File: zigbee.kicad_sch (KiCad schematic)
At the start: 49 parts, among them J201 Conn_Coaxial, J202 Conn_Coaxial, U201 0900PC15A0036E, U202 CC2652P1FRGZR, U203 CC2652P1FRGZR, X201 Crystal, X202 Crystal_GND24

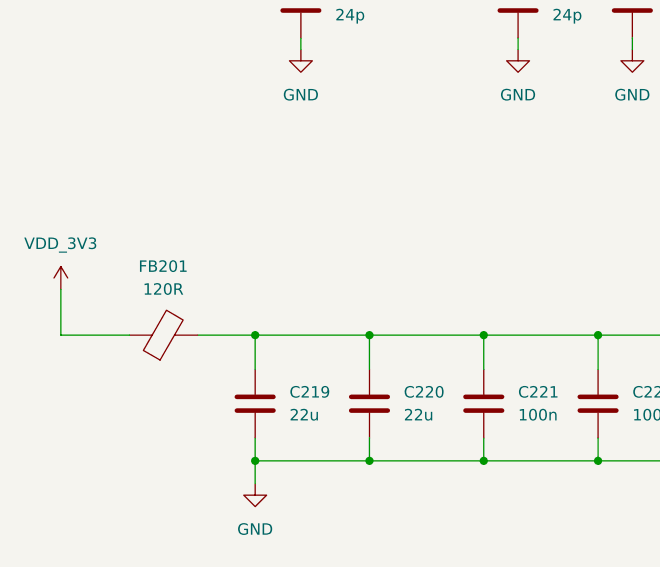
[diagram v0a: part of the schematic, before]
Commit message: Added more thread circuitry
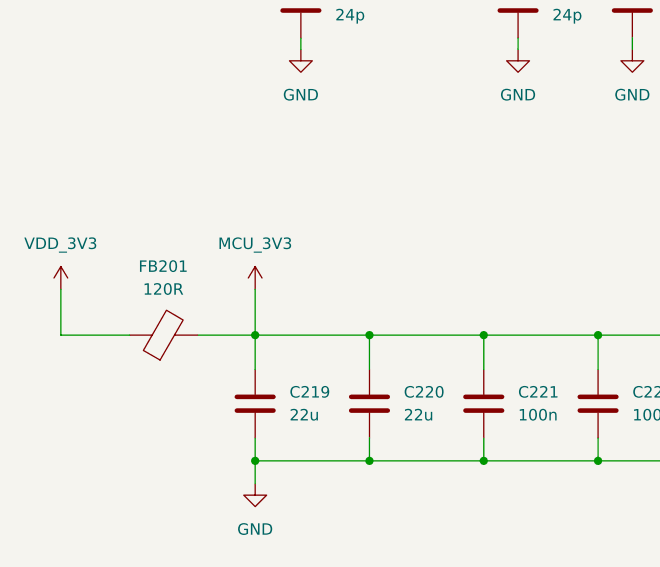
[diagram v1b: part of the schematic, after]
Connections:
- net MCU_3V3: now also C219.1, C220.1, C221.1, C222.1, C223.1, C224.1, FB201.2
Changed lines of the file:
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@@
 	(wire
 		(pts
+			(xy 54.61 177.8) (xy 54.61 182.88)
+		)
+		(stroke
+			(width 0)
+			(type default)
+		)
+	)
+	(wire
+		(pts
 			(xy 83.82 138.43) (xy 74.93 138.43)
 		)
@@
 					(unit 1)
 				)
+			)
+		)
+	)
+	(symbol
+		(lib_id "power:VDD")
+		(at 54.61 177.8 0)
+		(unit 1)
+		(exclude_from_sim no)
+		(in_bom yes)
+		(on_board yes)
+		(dnp no)
+		(fields_autoplaced yes)
+		(property "Reference" "#PWR0229"
+			(at 54.61 181.61 0)
+			(effects
+				(font
+					(size 1.27 1.27)
+				)
+				(hide yes)
+			)
+		)
+		(property "Value" "MCU_3V3"
+			(at 54.61 172.72 0)
+			(effects
+				(font
+					(size 1.27 1.27)
+				)
+			)
+		)
+		(property "Footprint" ""
+			(at 54.61 177.8 0)
+			(effects
+				(font
+					(size 1.27 1.27)
+				)
+				(hide yes)
+			)
+		)
+		(property "Datasheet" ""
+			(at 54.61 177.8 0)
+			(effects
+				(font
+					(size 1.27 1.27)
+				)
+				(hide yes)
+			)
+		)
+		(property "Description" "Power symbol creates a global label with name \"VDD\""
+			(at 54.61 177.8 0)
+			(effects
+				(font
+					(size 1.27 1.27)
+				)
+				(hide yes)
+			)
+		)
+		(pin "1"
+		)
+		(instances
+			(project "Leonhart"
+				(path "/b43b7bca-e50d-42ec-8ff0-e0016dfefe0a/4037e4ca-7763-453b-96d1-7d8342daaa99"
+					(reference "#PWR0229")
+					(unit 1)
+				)

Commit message: Fixed errors and added TI sysconfig file for AM6231
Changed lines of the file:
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@@
 		(dnp no)
 		(property "Reference" "R206"
-			(at 135.382 235.966 90)
+			(at 140.97 236.474 90)
 			(effects
 				(font
@@
 		)
 		(property "Value" "0R"
-			(at 145.796 235.966 90)
+			(at 140.716 233.68 90)
 			(effects
 				(font
@@
 		(dnp no)
 		(property "Reference" "R204"
-			(at 79.502 253.746 90)
+			(at 85.09 254.254 90)
 			(effects
 				(font
@@
 		)
 		(property "Value" "0R"
-			(at 89.916 253.746 90)
+			(at 84.836 251.46 90)
 			(effects
 				(font
@@
 		(dnp no)
 		(property "Reference" "R205"
-			(at 135.382 228.854 90)
+			(at 140.97 228.346 90)
 			(effects
 				(font
@@
 		)
 		(property "Value" "0R"
-			(at 145.796 228.854 90)
+			(at 140.716 231.14 90)
 			(effects
 				(font
@@
 		(dnp no)
 		(property "Reference" "R203"
-			(at 79.502 246.634 90)
+			(at 85.09 246.38 90)
 			(effects
 				(font
@@
 		)
 		(property "Value" "0R"
-			(at 89.916 246.634 90)
-			(effects
-				(font
+			(at 84.836 248.92 90)
+			(effects
+				(font

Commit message: Added more to sysconfig and wkup domain on schematic
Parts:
- R203, R206: value 0R -> 22R
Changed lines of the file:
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@@
 			)
 		)
-		(property "Value" "0R"
+		(property "Value" "22R"
 			(at 140.716 233.68 90)
 			(effects
@@
 			)
 		)
-		(property "Value" "0R"
+		(property "Value" "22R"
 			(at 84.836 248.92 90)
 			(effects

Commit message: Fixed balun matching network for CC2652P
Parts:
- removed J202: Conn_Coaxial, symbol Connector:Conn_Coaxial
- removed U201: 0900PC15A0036E, symbol SoftServicesSymbolLibrary:0900PC15A0036E
- added C227, C228: 1p, symbol Device:C
- added C229: 12p, symbol Device:C
- added C230: 470p, symbol Device:C
- added D201: D_TVS, symbol Device:D_TVS
- added J203: TC2050, Connector:Tag-Connect_TC2050-IDC-NL_2x05_P1.27mm_Vertical, symbol Connector:TC2050
- added L210, L211: 3.4n, symbol Device:L
- added R207, R208: 0R, symbol Device:R
- added U201: SKY13317-373, symbol SoftServicesSymbolLibrary:SKY13317-373
- C201, C204, C210: value 100p -> 1.5p
- C202, C221, C222, C223, C224, C225, C226: value 100n -> 0.1u
- C205: value 100p -> 0.5p
- C206: value 10n -> 1.5p
- C207: value 24p -> 12p
- C208: value 24p -> 15p
- C209: value 24p -> 1u
- C211: value 2.4p -> 12p
- C212: value 0.8p -> 12p
- C213, C214: value C -> 7.5p
- C215: value 3p -> 10n
- C216: value 4.7p -> 12p
- C217: value 2.4p -> 1p
- C218: value 3.9p -> 1p
- L202: value 12n -> 6.8n
- L203: value 1n -> 2.4n
- L204: value 27n -> 2.4n
- L205: value 4.7n -> 3.3n
- L206: value 1n -> 2.7n
- L207: value 12n -> 20n
- L208: value 3.9n -> 3.7n
- L209: value 2.5n -> 3.7n
- R203, R206: value 22R -> 0R
- X201: value Crystal -> 32.768kHz
- X202: value Crystal_GND24 -> 48MHz
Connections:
- net CC2652_RF_PA: now also U201.6 (V2)
- net CC2652_TCK: now also J203.4
- net CC2652_TDI: now also J203.8
- net CC2652_TDO: now also J203.6
- net CC2652_TMS: now also J203.2
- net GND: now also C204.1, C205.1, C206.1, C210.1, C212.1, C215.1, C227.1, C228.1, D201.1 (A1), J203.3, J203.5, U201.9 (EGP); no longer C204.2, C205.2, C206.2, C218.2, L209.1
- net RX/TX: no longer C204.1
- net at J201.1 (In): now also C230.2; no longer C201.1
- net at C212.2, C215.2: now also L203.2, R208.2; no longer L205.1, L208.2
- net at L203.1, U202.5 (TX_20DBM_P): now also C201.1, L202.1
- net at U202.1 (2_4_GHZ_RF_P): now also C218.1, L207.1, L208.1
- net at U202.2 (2_4_GHZ_RF_N): now also C217.1, L207.2, L209.1
- net CC2652_RESET_N: now reaches C202.1, R201.2, U202.35 (RESET_N)
- net CC2652_RESET_N: now also J203.10
- net at C214.1, X202.3: now also R207.2; no longer U202.46 (X48M_N)
- net at U202.6 (TX_20DBM_N): now also C204.2, L202.2, L204.1; no longer L206.1
- net CC2652_RF_2G4: now reaches U203.43 (DIO_30)
- net CC2652_RF_2G4: now also U201.7 (V3)
- net at C201.2: now also C205.2, L204.2, L205.1
- net at L209.2: now also C218.2, L210.1; no longer C215.1
- net MCU_3V3 renamed VDD3V3_CC
- net VDD3V3_CC: now also J203.1; no longer C205.1, C206.1, L202.2
- net VDDRF renamed VDDRF_CC
- net VDDRF_CC: now also R208.1
- new net: C227.2, L210.2, L211.1
- new net: R207.1, U202.46 (X48M_N)
- new net: C229.1, U201.8 (RF3)
- new net: C228.2, C229.2, L211.2
- new net: C206.2, L205.2, L206.1
- new net: C211.1, U201.5 (RF2)
- new net: C210.2, C211.2, L206.2
- new net: C230.1, D201.2 (A2), U201.1 (RFC)
- new net RX_TX: C216.2, L208.2
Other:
- note added: "Might need to pull V1 up or down"
- moved on the sheet: C202, C203, C207, C208, C209, C213, C214, C219, C220, C221, C222, C223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

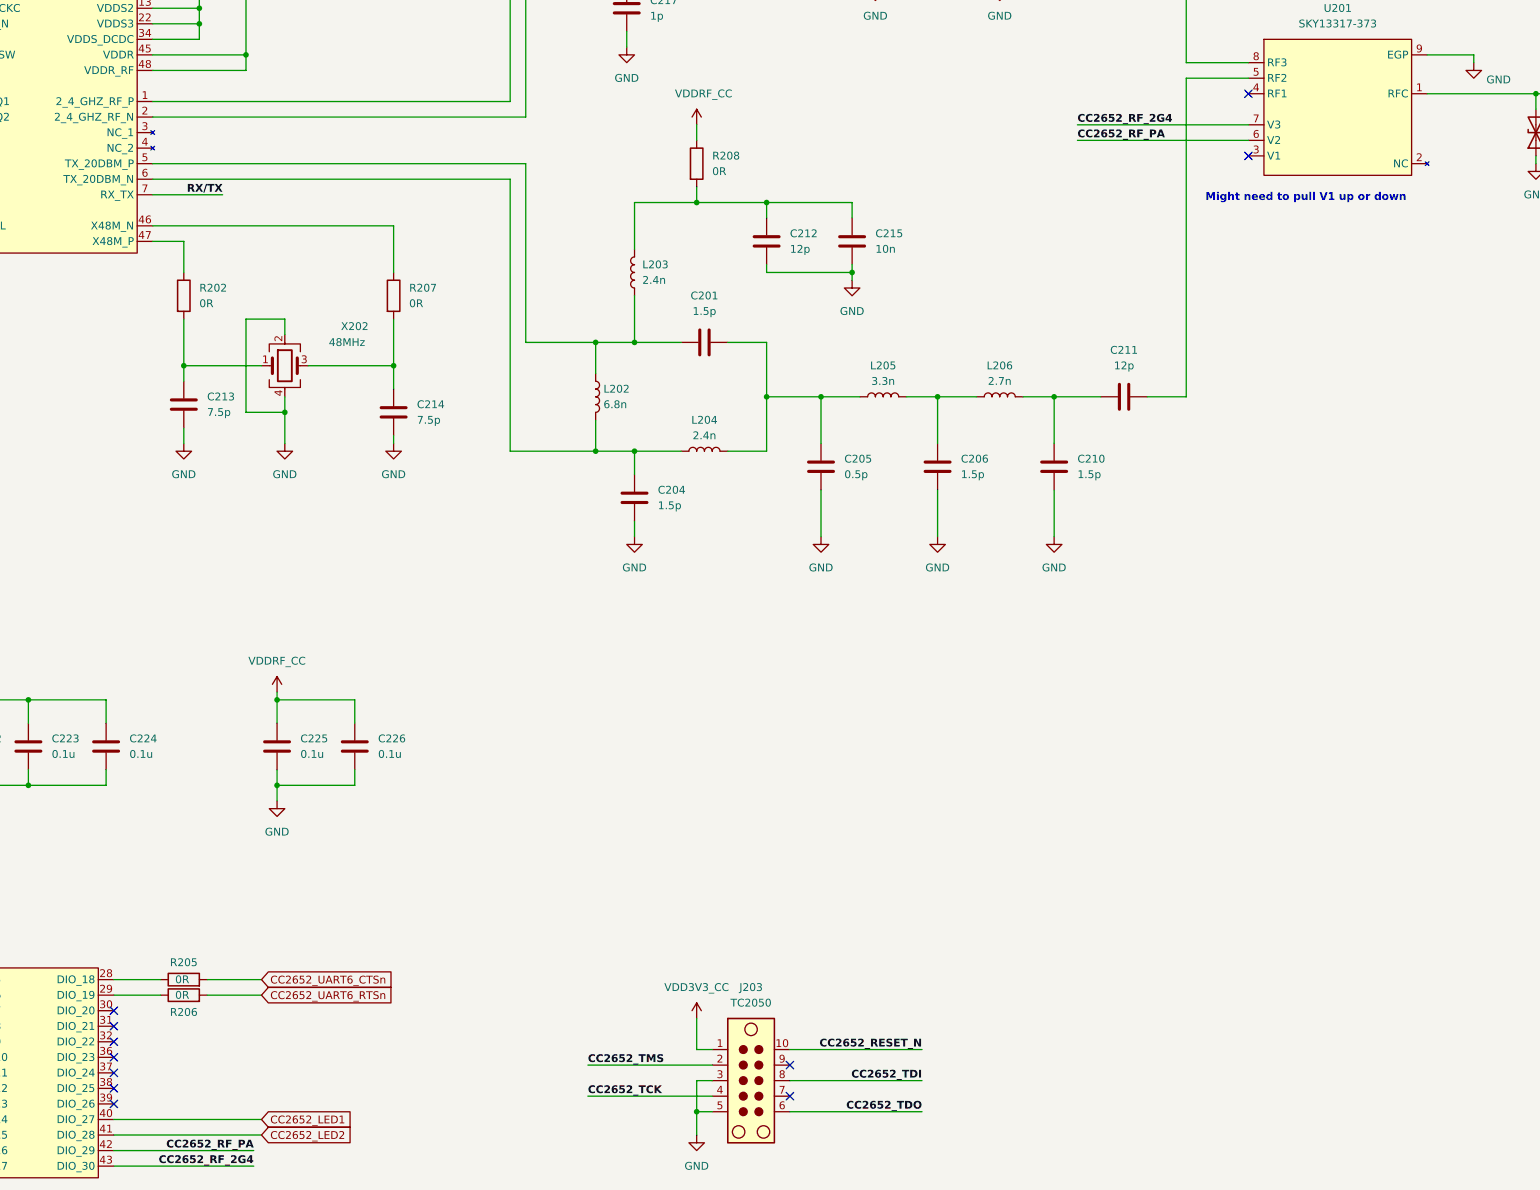
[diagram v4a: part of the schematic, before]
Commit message: Fixed net labels and added Ethernet reset digital logic. Also continued to update pinmux on TI sysconfig
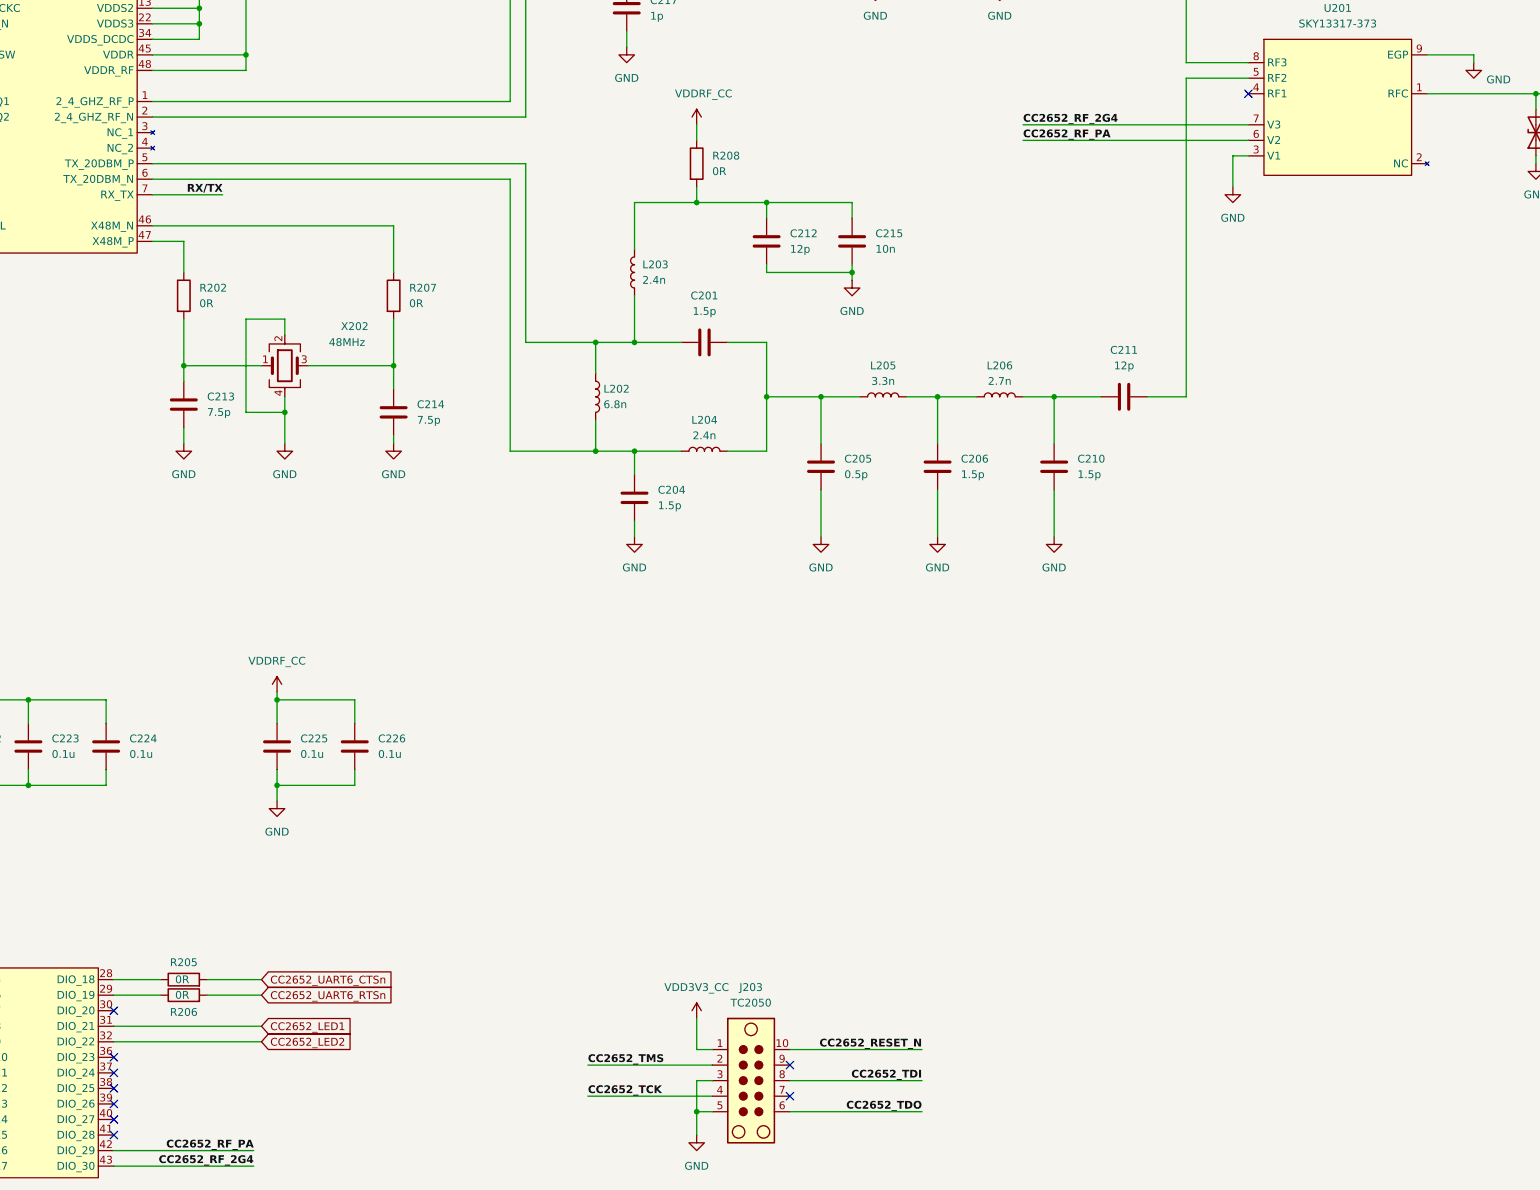
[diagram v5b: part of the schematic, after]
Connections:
- net CC2652_LED1: now also U203.31 (DIO_21); no longer U203.40 (DIO_27)
- net CC2652_LED2: now also U203.32 (DIO_22); no longer U203.41 (DIO_28)
- net GND: now also U201.3 (V1)
- no-connect marks 19 -> 18
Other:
- note removed: "Might need to pull V1 up or down"
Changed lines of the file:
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@@
 	(generator_version "9.0")
 	(paper "A2")
-	(text "Might need to pull V1 up or down"
-		(exclude_from_sim no)
-		(at 343.408 132.588 0)
-		(effects
-			(font
-				(size 1.27 1.27)
-				(thickness 0.254)
-				(bold yes)
-			)
-		)
-	)
 	(junction
 		(at 233.68 173.99)
@@
 	)
 	(no_connect
+		(at 148.59 283.21)
+	)
+	(no_connect
 		(at 334.01 115.57)
 	)
@@
 	)
 	(no_connect
-		(at 148.59 270.51)
-	)
-	(no_connect
 		(at 148.59 278.13)
 	)
@@
 	)
 	(no_connect
-		(at 334.01 125.73)
-	)
-	(no_connect
 		(at 148.59 265.43)
 	)
@@
 	)
 	(no_connect
+		(at 148.59 285.75)
+	)
+	(no_connect
 		(at 121.92 265.43)
 	)
@@
 		(at 259.08 274.32)
 	)
-	(no_connect
-		(at 148.59 267.97)
-	)
 	(wire
 		(pts
@@
 	(wire
 		(pts
-			(xy 148.59 283.21) (xy 172.72 283.21)
+			(xy 148.59 267.97) (xy 172.72 267.97)
 		)
 		(stroke
@@
 	(wire
 		(pts
-			(xy 148.59 285.75) (xy 172.72 285.75)
+			(xy 148.59 270.51) (xy 172.72 270.51)
 		)
 		(stroke
@@
 	(wire
 		(pts
-			(xy 306.07 120.65) (xy 334.01 120.65)
+			(xy 297.18 120.65) (xy 334.01 120.65)
 		)
 		(stroke
@@
 	(wire
 		(pts
+			(xy 331.47 130.81) (xy 331.47 125.73)
+		)
+		(stroke
+			(width 0)
+			(type default)
+		)
+	)
+	(wire
+		(pts
 			(xy 269.24 144.78) (xy 255.27 144.78)
 		)
@@
 	(wire
 		(pts
-			(xy 306.07 123.19) (xy 334.01 123.19)
+			(xy 297.18 123.19) (xy 334.01 123.19)
 		)
 		(stroke
@@
 	(wire
 		(pts
+			(xy 331.47 125.73) (xy 334.01 125.73)
+		)
+		(stroke
+			(width 0)
+			(type default)
+		)
+	)
+	(wire
+		(pts
 			(xy 96.52 218.44) (xy 96.52 214.63)
 		)
@@
 	)
 	(label "CC2652_RF_PA"
-		(at 306.07 123.19 0)
+		(at 297.18 123.19 0)
 		(effects
 			(font
@@
 	)
 	(label "CC2652_RF_2G4"
-		(at 306.07 120.65 0)
+		(at 297.18 120.65 0)
 		(effects
 			(font
@@
 	(global_label "CC2652_LED2"
 		(shape input)
-		(at 172.72 285.75 0)
+		(at 172.72 270.51 0)
 		(fields_autoplaced yes)
 		(effects
@@
 		)
 		(property "Intersheetrefs" "${INTERSHEET_REFS}"
-			(at 188.7074 285.75 0)
+			(at 188.7074 270.51 0)
 			(effects
 				(font
@@
 	(global_label "CC2652_LED1"
 		(shape input)
-		(at 172.72 283.21 0)
+		(at 172.72 267.97 0)
 		(fields_autoplaced yes)
 		(effects
@@
 		)
 		(property "Intersheetrefs" "${INTERSHEET_REFS}"
-			(at 188.7074 283.21 0)
+			(at 188.7074 267.97 0)
 			(effects
 				(font
@@
 					(unit 1)
 				)
+			)
+		)
+	)
+	(symbol
+		(lib_id "power:GND")
+		(at 331.47 130.81 0)
+		(unit 1)
+		(exclude_from_sim no)
+		(in_bom yes)
+		(on_board yes)
+		(dnp no)
+		(fields_autoplaced yes)
+		(property "Reference" "#PWR0234"
+			(at 331.47 137.16 0)
+			(effects
+				(font
+					(size 1.27 1.27)
+				)
+				(hide yes)
+			)
+		)
+		(property "Value" "GND"
+			(at 331.47 135.89 0)
+			(effects
+				(font
+					(size 1.27 1.27)
+				)
+			)
+		)
+		(property "Footprint" ""
+			(at 331.47 130.81 0)
+			(effects
+				(font
+					(size 1.27 1.27)
+				)
+				(hide yes)
+			)
+		)
+		(property "Datasheet" ""
+			(at 331.47 130.81 0)
+			(effects
+				(font
+					(size 1.27 1.27)
+				)
+				(hide yes)
+			)
+		)
+		(property "Description" "Power symbol creates a global label with name \"GND\" , ground"
+			(at 331.47 130.81 0)
+			(effects
+				(font
+					(size 1.27 1.27)
+				)
+				(hide yes)
+			)
+		)
+		(pin "1"
+		)
+		(instances
+			(project ""
+				(path "/b43b7bca-e50d-42ec-8ff0-e0016dfefe0a/4037e4ca-7763-453b-96d1-7d8342daaa99"
+					(reference "#PWR0234")
+					(unit 1)
+				)

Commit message: Tidied up schematic
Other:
- note added: "CC2652P IO Interface"
- note added: "CC2652P JTAG Interface + TagConnect"
- note added: "CC2652P Zigbee Network"
- note added: "Decoupling Capacitors"
- note added: "Need to configure GPIO for antenna to be connected to a path"
- moved on the sheet: C201, C202, C203, C204, C205, C206, C207, C208, C209, C210, C211, C212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

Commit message: Fixed small issues
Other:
- note added: "CC2652P I/O Interface"
- note removed: "CC2652P IO Interface"
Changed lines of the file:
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@@
 		)
 	)
-	(text "CC2652P IO Interface"
+	(text "CC2652P I/O Interface"
 		(exclude_from_sim no)
 		(at 274.828 243.586 0)
